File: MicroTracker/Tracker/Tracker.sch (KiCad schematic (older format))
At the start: 0 parts

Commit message: added connections
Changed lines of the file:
@@
 $EndDescr
 $Sheet
-S 8350 700  2450 800
+S 7800 3450 900  600
 U 5EF7F21E
 F0 "Power" 50
 F1 "Power.sch" 50
-F2 "v_bat_measure" I L 8350 800 50
-$EndSheet
-$Sheet
-S 8350 1700 2450 750
+F2 "v_bat_measure" I L 7800 3550 50
+$EndSheet
+$Sheet
+S 9850 3650 900  650
 U 5EF7F258
 F0 "GPS" 50
 F1 "GPS.sch" 50
-F2 "GPS_TX" I L 8350 1850 50
-F3 "GPS_RX" I L 8350 1950 50
-$EndSheet
-$Sheet
-S 8350 2650 2450 700
+F2 "GPS_TX" I L 9850 3800 50
+F3 "GPS_RX" I L 9850 3900 50
+$EndSheet
+$Sheet
+S 9850 4600 900  550
 U 5EF7F2B3
 F0 "Pressure" 50
 F1 "Pressure.sch" 50
-F2 "Pressure_SDA" I L 8350 2850 50
-F3 "Pressure_SCLK" I L 8350 2950 50
-$EndSheet
-$Sheet
-S 8350 3600 2500 800
+F2 "Pressure_SDA" I L 9850 4800 50
+F3 "Pressure_SCLK" I L 9850 4900 50
+$EndSheet
+$Sheet
+S 7850 4500 950  800
 U 5EF7F30A
 F0 "Transceiver" 50
 F1 "Transceiver.sch" 50
-F2 "Transceiver_SCLK" I L 8350 3700 50
-F3 "Transceiver_MISO" I L 8350 3800 50
-F4 "Transceiver_RESET" I L 8350 3900 50
-F5 "Transceiver_MOSI" I L 8350 4000 50
-F6 "Transceiver_TX" I L 8350 4300 50
-F7 "Transceiver_RX" I L 8350 4200 50
+F2 "Transceiver_SCLK" I L 7850 4600 50
+F3 "Transceiver_MISO" I L 7850 4700 50
+F4 "Transceiver_RESET" I L 7850 4800 50
+F5 "Transceiver_MOSI" I L 7850 4900 50
+F6 "Transceiver_TX" I L 7850 5200 50
+F7 "Transceiver_RX" I L 7850 5100 50
 $EndSheet
 $Sheet
@@
 $EndSheet
 $Sheet
-S 8350 4650 2500 750
+S 7850 5550 1000 700
 U 5EF834FA
 F0 "Sheet5EF834F9" 50
 F1 "USB.sch" 50
-F2 "USB_DTR" I L 8350 4800 50
-F3 "USB_RXD0" I L 8350 4900 50
-F4 "USB_TXD0" I L 8350 5000 50
-$EndSheet
-Text GLabel 8100 2850 0    50   Input ~ 0
+F2 "USB_DTR" I L 7850 5700 50
+F3 "USB_RXD0" I L 7850 5800 50
+F4 "USB_TXD0" I L 7850 5900 50
+$EndSheet
+Text GLabel 9600 4800 0    50   Input ~ 0
 Pressure_SDA
-Text GLabel 8100 2950 0    50   Input ~ 0
+Text GLabel 9600 4900 0    50   Input ~ 0
 Pressure_SCLK
-Text GLabel 8100 3700 0    50   Input ~ 0
+Text GLabel 7600 4600 0    50   Input ~ 0
 Transciever_SCLK
-Text GLabel 8100 3800 0    50   Input ~ 0
+Text GLabel 7600 4700 0    50   Input ~ 0
 Transciever_MISO
-Text GLabel 8100 3900 0    50   Input ~ 0
+Text GLabel 7600 4800 0    50   Input ~ 0
 Transciever_RESET
-Text GLabel 8100 4000 0    50   Input ~ 0
+Text GLabel 7600 4900 0    50   Input ~ 0
 Transciever_MOSI
 Wire Wire Line
-	8100 3700 8350 3700
-Wire Wire Line
-	8100 3800 8350 3800
-Wire Wire Line
-	8100 3900 8350 3900
-Wire Wire Line
-	8100 4000 8350 4000
-Text GLabel 8050 1850 0    50   Input ~ 0
+	7600 4600 7850 4600
+Wire Wire Line
+	7600 4700 7850 4700
+Wire Wire Line
+	7600 4800 7850 4800
+Wire Wire Line
+	7600 4900 7850 4900
+Text GLabel 9550 3800 0    50   Input ~ 0
 GPS_TX
-Text GLabel 8050 1950 0    50   Input ~ 0
+Text GLabel 9550 3900 0    50   Input ~ 0
 GPS_RX
 Wire Wire Line
-	8050 1850 8350 1850
-Wire Wire Line
-	8050 1950 8350 1950
-Text GLabel 8000 800  0    50   Input ~ 0
+	9550 3800 9850 3800
+Wire Wire Line
+	9550 3900 9850 3900
+Text GLabel 7450 3550 0    50   Input ~ 0
 v_bat_measure
 Wire Wire Line
-	8000 800  8350 800
-Wire Wire Line
-	8100 2850 8350 2850
-Wire Wire Line
-	8100 2950 8350 2950
+	7450 3550 7800 3550
+Wire Wire Line
+	9600 4800 9850 4800
+Wire Wire Line
+	9600 4900 9850 4900
 Text GLabel 5100 3500 2    50   Input ~ 0
 Pressure_SDA
@@
 v_bat_measure
 $Sheet
-S 8350 5600 2500 750
+S 9800 5550 1050 750
 U 5EF91B46
 F0 "Storage" 50
 F1 "Storage.sch" 50
-F2 "SD_CLK" I L 8350 5750 50
-F3 "SD_MISO" I L 8350 5850 50
-F4 "SD_CS" I L 8350 5950 50
-F5 "SD_MOSI" I L 8350 6050 50
-$EndSheet
-Text GLabel 8200 4900 0    50   Input ~ 0
+F2 "SD_CLK" I L 9800 5700 50
+F3 "SD_MISO" I L 9800 5800 50
+F4 "SD_CS" I L 9800 5900 50
+F5 "SD_MOSI" I L 9800 6000 50
+$EndSheet
+Text GLabel 7700 5800 0    50   Input ~ 0
 USB_RXD0
-Text GLabel 8200 4800 0    50   Input ~ 0
+Text GLabel 7700 5700 0    50   Input ~ 0
 USB_DTR
-Text GLabel 8200 5000 0    50   Input ~ 0
+Text GLabel 7700 5900 0    50   Input ~ 0
 USB_TXD0
 Text GLabel 5050 5050 2    50   Input ~ 0
@@
 USB_TXD0
 Wire Wire Line
-	8200 4800 8350 4800
-Wire Wire Line
-	8200 4900 8350 4900
-Wire Wire Line
-	8200 5000 8350 5000
+	7700 5700 7850 5700
+Wire Wire Line
+	7700 5800 7850 5800
+Wire Wire Line
+	7700 5900 7850 5900
 Wire Wire Line
 	5050 4950 4950 4950
 Wire Wire Line
 	4950 5050 5050 5050
-Text GLabel 8100 4200 0    50   Input ~ 0
+Text GLabel 7600 5100 0    50   Input ~ 0
 Transceiver_RX
-Text GLabel 8100 4300 0    50   Input ~ 0
+Text GLabel 7600 5200 0    50   Input ~ 0
 Transceiver_RX
 Wire Wire Line
-	8100 4200 8350 4200
-Wire Wire Line
-	8100 4300 8350 4300
+	7600 5100 7850 5100
+Wire Wire Line
+	7600 5200 7850 5200
 Text GLabel 5100 1750 2    50   Input ~ 0
 Transceiver_RX
@@
 Transceiver_TX
 $Sheet
-S 4050 6600 2650 950
+S 7800 1600 1050 1000
 U 5EFA735D
 F0 "Charges" 50
@@
 	4950 2100 5100 2100
 $Sheet
-S 600  6600 3000 950
+S 9400 2050 1150 750
 U 5F07F54B
 F0 "9_DOF" 50
 F1 "9_DOF.sch" 50
-F2 "9DofSDA" I R 3600 6750 50
-F3 "9DofSCL" I R 3600 6850 50
-F4 "9DofSDOM" I R 3600 7000 50
-F5 "9DofAG" I R 3600 7100 50
-$EndSheet
-Text GLabel 4250 5800 0    50   Input ~ 0
+F2 "9DofSDA" I R 10550 2200 50
+F3 "9DofSCL" I R 10550 2300 50
+F4 "9DofSDOM" I R 10550 2450 50
+F5 "9DofAG" I R 10550 2550 50
+$EndSheet
+Text GLabel 10650 2200 2    50   Input ~ 0
 9DofSDA
-Text GLabel 4250 5900 0    50   Input ~ 0
+Text GLabel 10650 2300 2    50   Input ~ 0
 9DofSCL
 Text GLabel 5100 3400 2    50   Input ~ 0
@@
 Wire Wire Line
 	5000 3900 5000 4000
+Text GLabel 9650 5700 0    50   Input ~ 0
+SD_CLK
+Text GLabel 9650 5800 0    50   Input ~ 0
+SD_MISO
+Text GLabel 9650 5900 0    50   Input ~ 0
+SD_CS
+Text GLabel 9650 6000 0    50   Input ~ 0
+SD_MOSI
+Wire Wire Line
+	9650 5700 9800 5700
+Wire Wire Line
+	9650 5800 9800 5800
+Wire Wire Line
+	9650 5900 9800 5900
+Wire Wire Line
+	9650 6000 9800 6000
+Text GLabel 5100 2750 2    50   Input ~ 0
+SD_CLK
+Text GLabel 5100 2850 2    50   Input ~ 0
+SD_MISO
+Text GLabel 5100 2950 2    50   Input ~ 0
+SD_CS
+Text GLabel 5100 3050 2    50   Input ~ 0
+SD_MOSI
+Wire Wire Line
+	4950 2750 5100 2750
+Wire Wire Line
+	4950 2850 5100 2850
+Wire Wire Line
+	4950 2950 5100 2950
+Wire Wire Line
+	4950 3050 5100 3050
+Wire Wire Line
+	10550 2200 10650 2200
+Wire Wire Line
+	10550 2300 10650 2300
 $EndSCHEMATC

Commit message: added charges
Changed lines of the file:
@@
 F2 "GPS_TX" I L 9850 3800 50
 F3 "GPS_RX" I L 9850 3900 50
+F4 "GPS_RESET" I L 9850 4000 50
+F5 "GPS_WAKE_UP" I L 9850 4100 50
+F6 "GPS_SCL" I L 9850 4200 50
+F7 "GPS_SDA" I L 9850 3700 50
 $EndSheet
 $Sheet
@@
 F13 "SD_CS" I R 4950 2950 50
 F14 "SD_MOSI" I R 4950 3050 50
+F15 "charge1Trigger" I R 4950 4250 50
+F16 "charge2Trigger" I R 4950 4350 50
+F17 "charge2Sense" I R 4950 4550 50
+F18 "charge1Sense" I R 4950 4650 50
 $EndSheet
 $Sheet
@@
 Transceiver_TX
 $Sheet
-S 7800 1600 1050 1000
+S 7700 950  1050 1000
 U 5EFA735D
 F0 "Charges" 50
 F1 "Charges.sch" 50
+F2 "charge1Trigger" I L 7700 1150 50
+F3 "charge2Trigger" I L 7700 1250 50
+F4 "charge2Sense" I L 7700 1550 50
+F5 "charge1Sense" I L 7700 1450 50
 $EndSheet
 Wire Wire Line
@@
 	4950 2100 5100 2100
 $Sheet
-S 9400 2050 1150 750
+S 9300 1400 1150 750
 U 5F07F54B
 F0 "9_DOF" 50
 F1 "9_DOF.sch" 50
-F2 "9DofSDA" I R 10550 2200 50
-F3 "9DofSCL" I R 10550 2300 50
-F4 "9DofSDOM" I R 10550 2450 50
-F5 "9DofAG" I R 10550 2550 50
-$EndSheet
-Text GLabel 10650 2200 2    50   Input ~ 0
+F2 "9DofSDA" I R 10450 1550 50
+F3 "9DofSCL" I R 10450 1650 50
+F4 "9DofSDOM" I R 10450 1800 50
+F5 "9DofAG" I R 10450 1900 50
+$EndSheet
+Text GLabel 10550 1550 2    50   Input ~ 0
 9DofSDA
-Text GLabel 10650 2300 2    50   Input ~ 0
+Text GLabel 10550 1650 2    50   Input ~ 0
 9DofSCL
 Text GLabel 5100 3400 2    50   Input ~ 0
@@
 	4950 3050 5100 3050
 Wire Wire Line
-	10550 2200 10650 2200
-Wire Wire Line
-	10550 2300 10650 2300
+	10450 1550 10550 1550
+Wire Wire Line
+	10450 1650 10550 1650
 $EndSCHEMATC

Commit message: assigned parts
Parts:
- added H1, H2, H3, H4: MountingHole_Pad, MountingHole:MountingHole_3.5mm_Pad, symbol Mechanical:MountingHole_Pad
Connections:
- new net GND: H1.1, H2.1, H3.1, H4.1
- no-connect marks 0 -> 1
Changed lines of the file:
@@
 Text GLabel 7700 5800 0    50   Input ~ 0
 USB_RXD0
-Text GLabel 7700 5700 0    50   Input ~ 0
-USB_DTR
 Text GLabel 7700 5900 0    50   Input ~ 0
 USB_TXD0
@@
 Text GLabel 5100 2750 2    50   Input ~ 0
 SD_CLK
-Text GLabel 5100 2850 2    50   Input ~ 0
+Text GLabel 5100 3050 2    50   Input ~ 0
 SD_MISO
 Text GLabel 5100 2950 2    50   Input ~ 0
 SD_CS
-Text GLabel 5100 3050 2    50   Input ~ 0
+Text GLabel 5100 2850 2    50   Input ~ 0
 SD_MOSI
 Wire Wire Line
@@
 Wire Wire Line
 	10450 1650 10550 1650
+NoConn ~ 7700 5700
+$Comp
+L Mechanical:MountingHole_Pad H1
+U 1 1 5F16E7C3
+P 800 7300
+F 0 "H1" H 900 7349 50  0000 L CNN
+F 1 "MountingHole_Pad" H 900 7258 50  0000 L CNN
+F 2 "MountingHole:MountingHole_3.5mm_Pad" H 800 7300 50  0001 C CNN
+F 3 "~" H 800 7300 50  0001 C CNN
+	1    800  7300
+	1    0    0    -1
+$EndComp
+$Comp
+L power:GND #PWR0171
+U 1 1 5F16ECAC
+P 800 7500
+F 0 "#PWR0171" H 800 7250 50  0001 C CNN
+F 1 "GND" H 805 7327 50  0000 C CNN
+F 2 "" H 800 7500 50  0001 C CNN
+F 3 "" H 800 7500 50  0001 C CNN
+	1    800  7500
+	1    0    0    -1
+$EndComp
+Wire Wire Line
+	800  7500 800  7400
+$Comp
+L Mechanical:MountingHole_Pad H2
+U 1 1 5F17171F
+P 1700 7300
+F 0 "H2" H 1800 7349 50  0000 L CNN
+F 1 "MountingHole_Pad" H 1800 7258 50  0000 L CNN
+F 2 "MountingHole:MountingHole_3.5mm_Pad" H 1700 7300 50  0001 C CNN
+F 3 "~" H 1700 7300 50  0001 C CNN
+	1    1700 7300
+	1    0    0    -1
+$EndComp
+$Comp
+L power:GND #PWR0172
+U 1 1 5F171725
+P 1700 7500
+F 0 "#PWR0172" H 1700 7250 50  0001 C CNN
+F 1 "GND" H 1705 7327 50  0000 C CNN
+F 2 "" H 1700 7500 50  0001 C CNN
+F 3 "" H 1700 7500 50  0001 C CNN
+	1    1700 7500
+	1    0    0    -1
+$EndComp
+Wire Wire Line
+	1700 7500 1700 7400
+$Comp
+L Mechanical:MountingHole_Pad H3
+U 1 1 5F17331D
+P 2600 7300
+F 0 "H3" H 2700 7349 50  0000 L CNN
+F 1 "MountingHole_Pad" H 2700 7258 50  0000 L CNN
+F 2 "MountingHole:MountingHole_3.5mm_Pad" H 2600 7300 50  0001 C CNN
+F 3 "~" H 2600 7300 50  0001 C CNN
+	1    2600 7300
+	1    0    0    -1
+$EndComp
+$Comp
+L power:GND #PWR0173
+U 1 1 5F173323
+P 2600 7500
+F 0 "#PWR0173" H 2600 7250 50  0001 C CNN
+F 1 "GND" H 2605 7327 50  0000 C CNN
+F 2 "" H 2600 7500 50  0001 C CNN
+F 3 "" H 2600 7500 50  0001 C CNN
+	1    2600 7500
+	1    0    0    -1
+$EndComp
+Wire Wire Line
+	2600 7500 2600 7400
+$Comp
+L Mechanical:MountingHole_Pad H4
+U 1 1 5F17332A
+P 3500 7300
+F 0 "H4" H 3600 7349 50  0000 L CNN
+F 1 "MountingHole_Pad" H 3600 7258 50  0000 L CNN
+F 2 "MountingHole:MountingHole_3.5mm_Pad" H 3500 7300 50  0001 C CNN
+F 3 "~" H 3500 7300 50  0001 C CNN
+	1    3500 7300
+	1    0    0    -1
+$EndComp
+$Comp
+L power:GND #PWR0174
+U 1 1 5F173330
+P 3500 7500
+F 0 "#PWR0174" H 3500 7250 50  0001 C CNN
+F 1 "GND" H 3505 7327 50  0000 C CNN
+F 2 "" H 3500 7500 50  0001 C CNN
+F 3 "" H 3500 7500 50  0001 C CNN
+	1    3500 7500
+	1    0    0    -1
+$EndComp
+Wire Wire Line
+	3500 7500 3500 7400
 $EndSCHEMATC

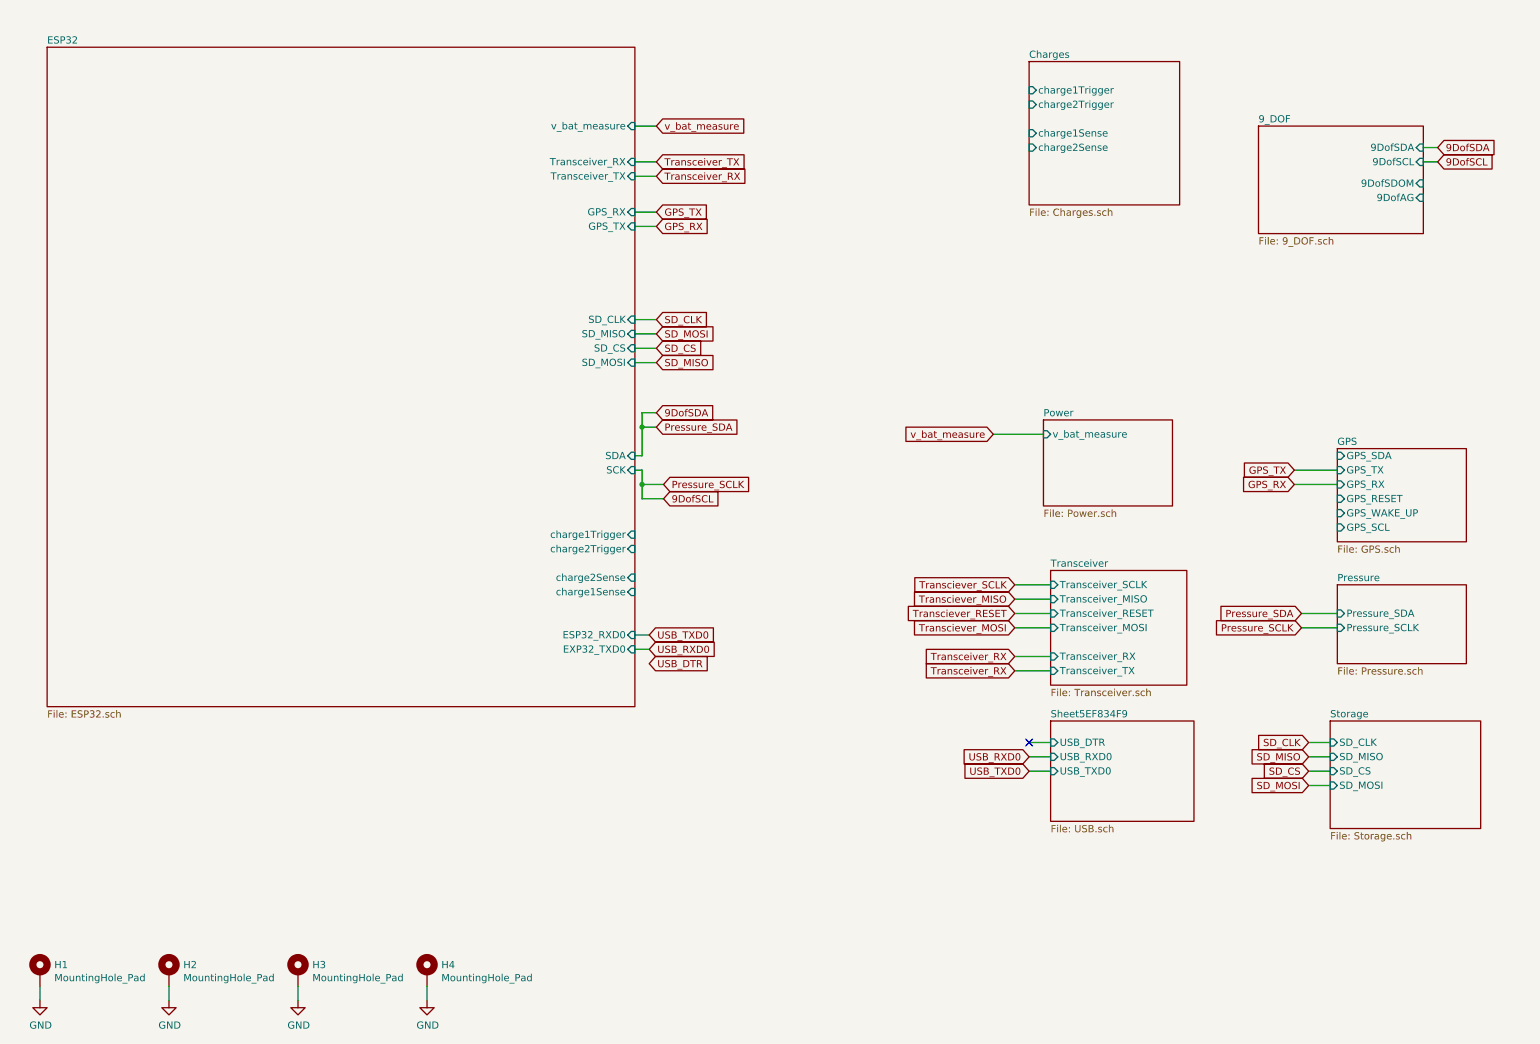
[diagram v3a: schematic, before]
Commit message: added more parts and lib
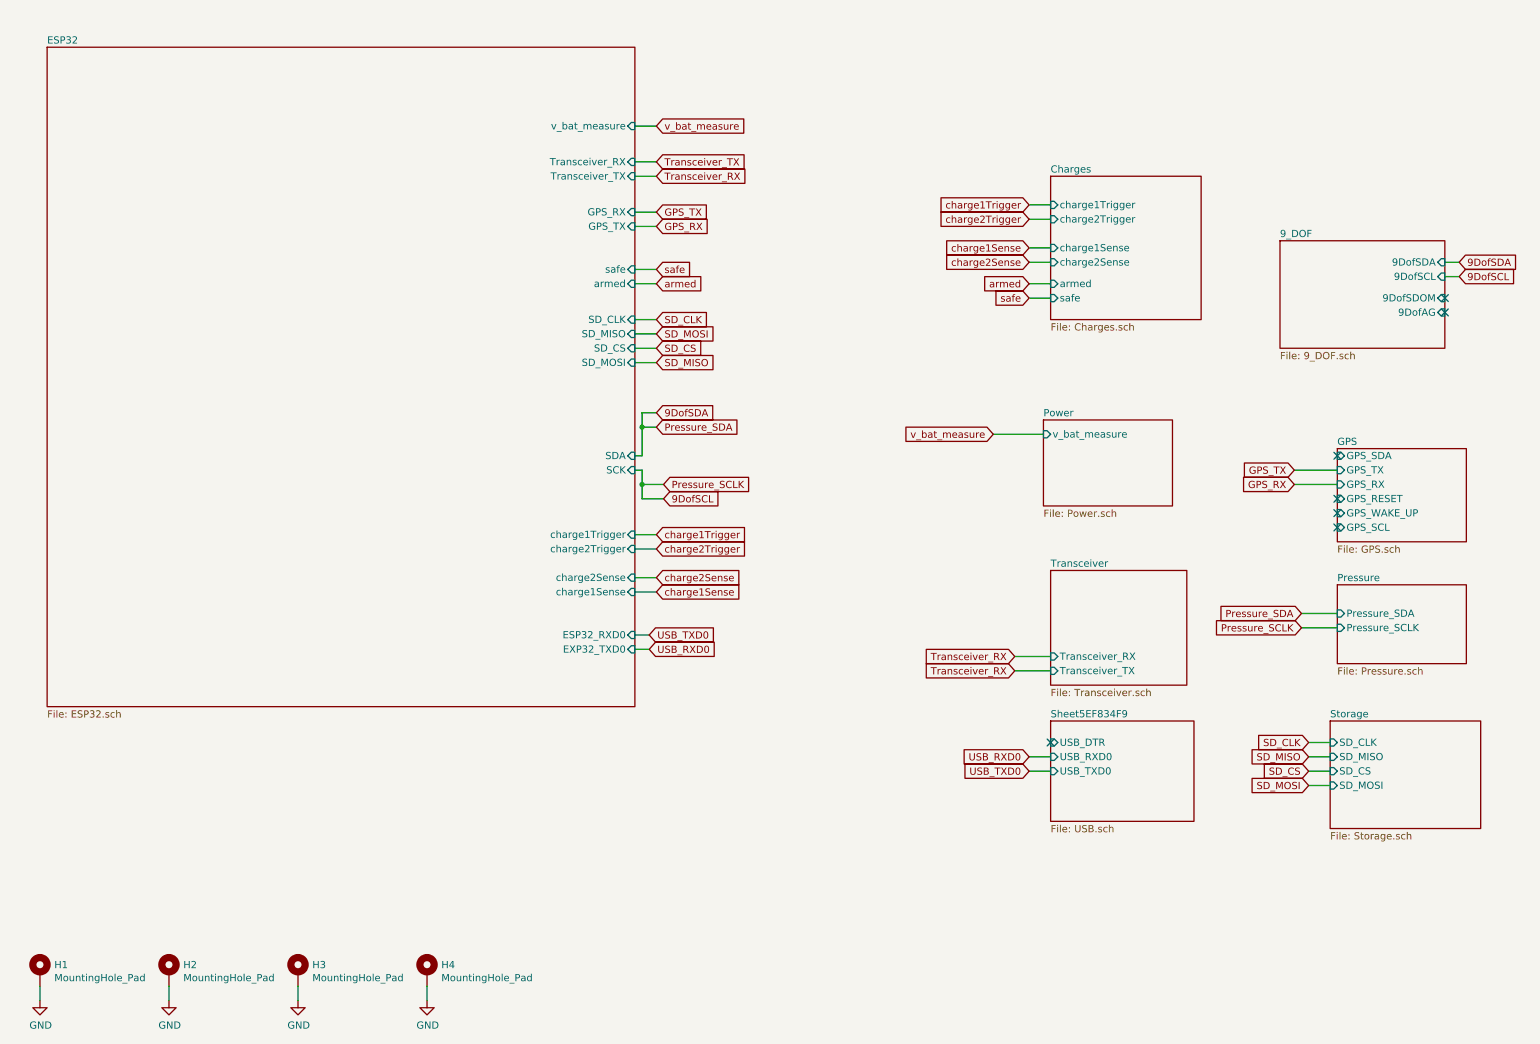
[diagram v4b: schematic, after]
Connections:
- no-connect marks 1 -> 7
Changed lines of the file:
@@
 F0 "Transceiver" 50
 F1 "Transceiver.sch" 50
-F2 "Transceiver_SCLK" I L 7850 4600 50
-F3 "Transceiver_MISO" I L 7850 4700 50
-F4 "Transceiver_RESET" I L 7850 4800 50
-F5 "Transceiver_MOSI" I L 7850 4900 50
-F6 "Transceiver_TX" I L 7850 5200 50
-F7 "Transceiver_RX" I L 7850 5100 50
+F2 "Transceiver_TX" I L 7850 5200 50
+F3 "Transceiver_RX" I L 7850 5100 50
 $EndSheet
 $Sheet
@@
 F17 "charge2Sense" I R 4950 4550 50
 F18 "charge1Sense" I R 4950 4650 50
+F19 "armed" I R 4950 2500 50
+F20 "safe" I R 4950 2400 50
 $EndSheet
 $Sheet
@@
 Text GLabel 9600 4900 0    50   Input ~ 0
 Pressure_SCLK
-Text GLabel 7600 4600 0    50   Input ~ 0
-Transciever_SCLK
-Text GLabel 7600 4700 0    50   Input ~ 0
-Transciever_MISO
-Text GLabel 7600 4800 0    50   Input ~ 0
-Transciever_RESET
-Text GLabel 7600 4900 0    50   Input ~ 0
-Transciever_MOSI
-Wire Wire Line
-	7600 4600 7850 4600
-Wire Wire Line
-	7600 4700 7850 4700
-Wire Wire Line
-	7600 4800 7850 4800
-Wire Wire Line
-	7600 4900 7850 4900
 Text GLabel 9550 3800 0    50   Input ~ 0
 GPS_TX
@@
 Text GLabel 5050 5050 2    50   Input ~ 0
 USB_RXD0
-Text GLabel 5050 5150 2    50   Input ~ 0
-USB_DTR
 Text GLabel 5050 4950 2    50   Input ~ 0
 USB_TXD0
-Wire Wire Line
-	7700 5700 7850 5700
 Wire Wire Line
 	7700 5800 7850 5800
@@
 Transceiver_TX
 $Sheet
-S 7700 950  1050 1000
+S 7850 1750 1050 1000
 U 5EFA735D
 F0 "Charges" 50
 F1 "Charges.sch" 50
-F2 "charge1Trigger" I L 7700 1150 50
-F3 "charge2Trigger" I L 7700 1250 50
-F4 "charge2Sense" I L 7700 1550 50
-F5 "charge1Sense" I L 7700 1450 50
+F2 "charge1Trigger" I L 7850 1950 50
+F3 "charge2Trigger" I L 7850 2050 50
+F4 "charge2Sense" I L 7850 2350 50
+F5 "charge1Sense" I L 7850 2250 50
+F6 "armed" I L 7850 2500 50
+F7 "safe" I L 7850 2600 50
 $EndSheet
 Wire Wire Line
 	4950 1400 5100 1400
 Wire Wire Line
-	4950 1650 5100 1650
-Wire Wire Line
 	4950 1750 5100 1750
 Wire Wire Line
@@
 	4950 2100 5100 2100
 $Sheet
-S 9300 1400 1150 750
+S 9450 2200 1150 750
 U 5F07F54B
 F0 "9_DOF" 50
 F1 "9_DOF.sch" 50
-F2 "9DofSDA" I R 10450 1550 50
-F3 "9DofSCL" I R 10450 1650 50
-F4 "9DofSDOM" I R 10450 1800 50
-F5 "9DofAG" I R 10450 1900 50
-$EndSheet
-Text GLabel 10550 1550 2    50   Input ~ 0
+F2 "9DofSDA" I R 10600 2350 50
+F3 "9DofSCL" I R 10600 2450 50
+F4 "9DofSDOM" I R 10600 2600 50
+F5 "9DofAG" I R 10600 2700 50
+$EndSheet
+Text GLabel 10700 2350 2    50   Input ~ 0
 9DofSDA
-Text GLabel 10550 1650 2    50   Input ~ 0
+Text GLabel 10700 2450 2    50   Input ~ 0
 9DofSCL
 Text GLabel 5100 3400 2    50   Input ~ 0
@@
 	4950 3050 5100 3050
 Wire Wire Line
-	10450 1550 10550 1550
-Wire Wire Line
-	10450 1650 10550 1650
-NoConn ~ 7700 5700
+	10600 2350 10700 2350
+Wire Wire Line
+	10600 2450 10700 2450
 $Comp
 L Mechanical:MountingHole_Pad H1
@@
 Wire Wire Line
 	3500 7500 3500 7400
+Text GLabel 5100 4250 2    50   Input ~ 0
+charge1Trigger
+Text GLabel 5100 4350 2    50   Input ~ 0
+charge2Trigger
+Text GLabel 5100 4550 2    50   Input ~ 0
+charge2Sense
+Text GLabel 5100 4650 2    50   Input ~ 0
+charge1Sense
+Wire Wire Line
+	4950 4250 5100 4250
+Wire Wire Line
+	4950 4350 5100 4350
+Wire Wire Line
+	4950 4550 5100 4550
+Wire Wire Line
+	4950 4650 5100 4650
+Text GLabel 7700 1950 0    50   Input ~ 0
+charge1Trigger
+Text GLabel 7700 2050 0    50   Input ~ 0
+charge2Trigger
+Text GLabel 7700 2350 0    50   Input ~ 0
+charge2Sense
+Text GLabel 7700 2250 0    50   Input ~ 0
+charge1Sense
+Wire Wire Line
+	7700 1950 7850 1950
+Wire Wire Line
+	7700 2050 7850 2050
+Wire Wire Line
+	7700 2250 7850 2250
+Wire Wire Line
+	7700 2350 7850 2350
+NoConn ~ 9850 3700
+NoConn ~ 9850 4000
+NoConn ~ 9850 4100
+NoConn ~ 9850 4200
+NoConn ~ 7850 5700
+Wire Wire Line
+	4950 1650 5100 1650
+Text GLabel 7700 2500 0    50   Input ~ 0
+armed
+Text GLabel 7700 2600 0    50   Input ~ 0
+safe
+Wire Wire Line
+	7700 2500 7850 2500
+Wire Wire Line
+	7700 2600 7850 2600
+Text GLabel 5100 2500 2    50   Input ~ 0
+armed
+Text GLabel 5100 2400 2    50   Input ~ 0
+safe
+Wire Wire Line
+	4950 2400 5100 2400
+Wire Wire Line
+	4950 2500 5100 2500
+NoConn ~ 10600 2600
+NoConn ~ 10600 2700
 $EndSCHEMATC
